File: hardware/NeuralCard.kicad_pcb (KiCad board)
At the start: 2 copper layers, 85.6 x 54 mm, 66 parts, among them J1 ProgPads, J2 TYPE-C-31-M-12, Q1 AO3401A, SW1 SW-SMD_4P-L5.1-W5.1-P3.70-LS6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, SW2 SW-SMD_4P-L5.1-W5.1-P3.70-LS6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, SW3 SW_SPDT_Shouhan_MSK12C02, U1 WIRELM-SMD_ESP32-S3-WROOM-1, U2 LGA-14_L3.0-W2.5-P0.50-TL, U3 ME6211C33M5G-N, U4 SO-8_L4.9-W3.9-P1.27-LS5.9-BL, U5 USBLC6-2SC6

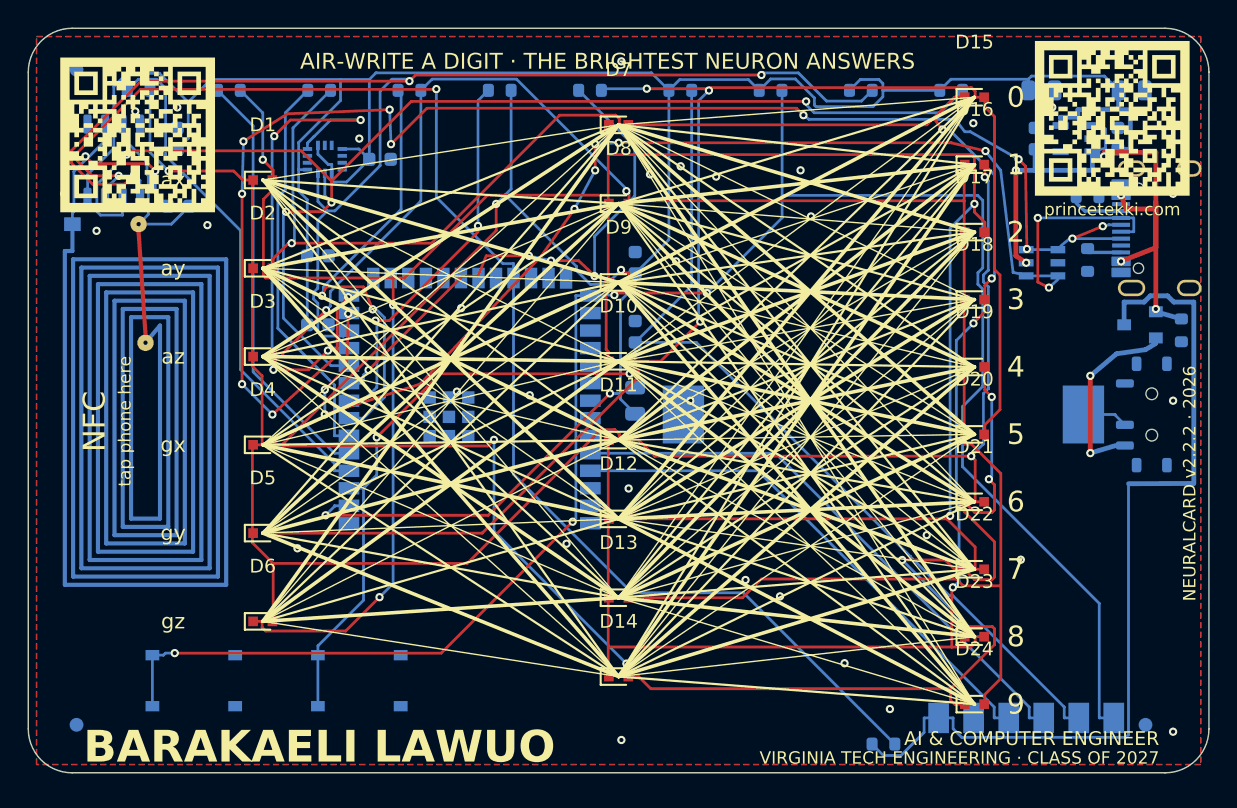
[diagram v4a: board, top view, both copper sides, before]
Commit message: bridge gnd islands
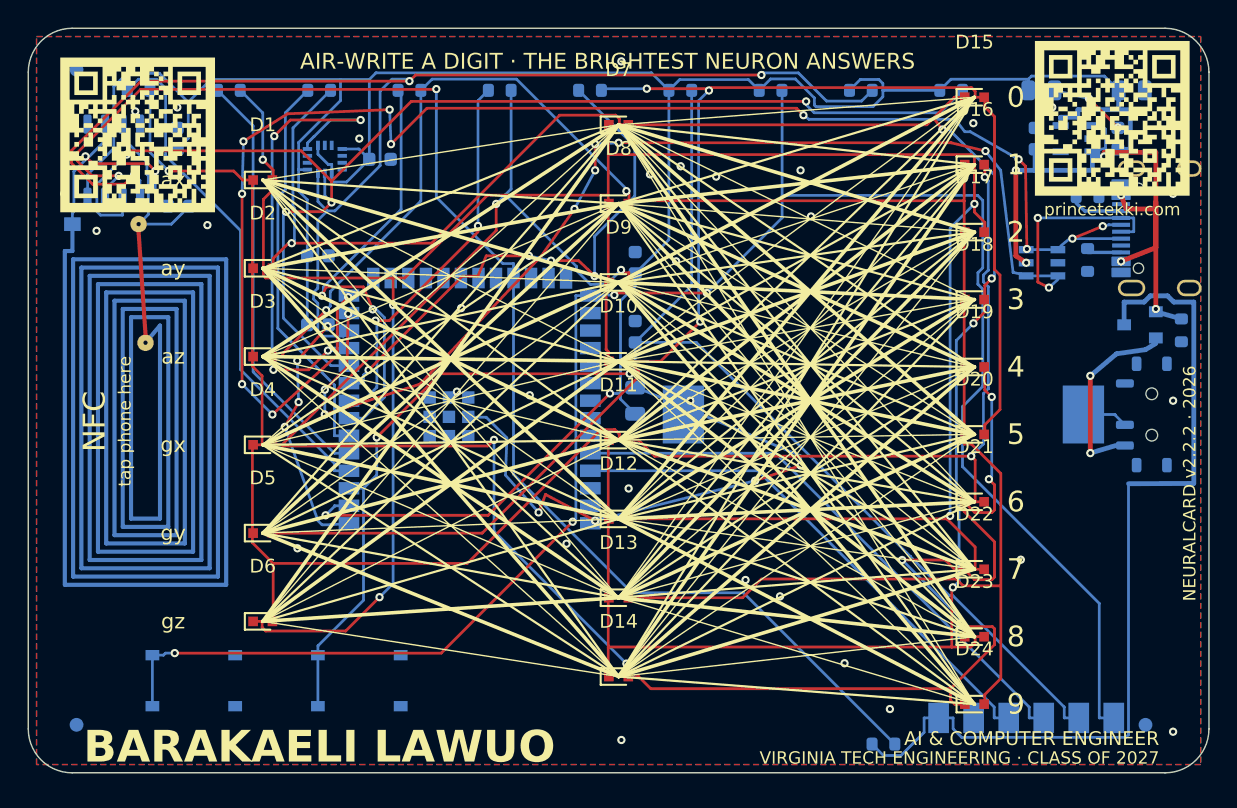
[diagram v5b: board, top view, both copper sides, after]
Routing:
- net GND: track 0.00 -> 67.9 mm, vias 32 -> 41
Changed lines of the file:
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@@
 			)
 		)
-		(clearance 0.09)
+		(clearance 0.1)
 		(attr smd)
 		(duplicate_pad_numbers_are_jumpers no)
@@
 		(net "USB_DP")
 	)
+	(segment
+		(start 56 31.7)
+		(end 52.7 32.8)
+		(width 0.2)
+		(layer "F.Cu")
+		(net "GND")
+	)
+	(segment
+		(start 21.7 21.6)
+		(end 19.5 24.1)
+		(width 0.2)
+		(layer "F.Cu")
+		(net "GND")
+	)
+	(segment
+		(start 41.1 35.7)
+		(end 37.5 33.8)
+		(width 0.2)
+		(layer "F.Cu")
+		(net "GND")
+	)
+	(segment
+		(start 19.6 27.1)
+		(end 18.6 28.9)
+		(width 0.2)
+		(layer "F.Cu")
+		(net "GND")
+	)
+	(segment
+		(start 37.5 33.8)
+		(end 37 35.1)
+		(width 0.2)
+		(layer "F.Cu")
+		(net "GND")
+	)
+	(segment
+		(start 79 7.2)
+		(end 76.9 5.1)
+		(width 0.2)
+		(layer "F.Cu")
+		(net "GND")
+	)
+	(via
+		(at 76.9 5.1)
+		(size 0.6)
+		(drill 0.3)
+		(layers "F.Cu" "B.Cu")
+		(net "GND")
+	)
 	(via
 		(at 10.806 5.734)
@@
 	)
 	(via
+		(at 79 7.2)
+		(size 0.6)
+		(drill 0.3)
+		(layers "F.Cu" "B.Cu")
+		(net "GND")
+	)
+	(via
 		(at 43 2.4)
 		(size 0.6)
@@
 	)
 	(via
+		(at 37 35.1)
+		(size 0.6)
+		(drill 0.3)
+		(layers "F.Cu" "B.Cu")
+		(net "GND")
+	)
+	(via
 		(at 7.758 6.026)
 		(size 0.6)
@@
 	)
 	(via
-		(at 65.139356 36.750118)
+		(at 43 51.6)
+		(size 0.6)
+		(drill 0.3)
+		(layers "F.Cu" "B.Cu")
+		(net "GND")
+	)
+	(via
+		(at 19.6 27.1)
 		(size 0.6)
 		(drill 0.3)
@@
 	)
 	(via
-		(at 43 51.6)
+		(at 52.7 32.8)
+		(size 0.6)
+		(drill 0.3)
+		(layers "F.Cu" "B.Cu")
+		(net "GND")
+	)
+	(via
+		(at 41.1 35.7)
 		(size 0.6)
 		(drill 0.3)
@@
 	)
 	(via
+		(at 19.5 24.1)
+		(size 0.6)
+		(drill 0.3)
+		(layers "F.Cu" "B.Cu")
+		(net "GND")
+	)
+	(via
 		(at 4.95 14.684853)
 		(size 0.6)
@@
 	)
 	(via
+		(at 56 31.7)
+		(size 0.6)
+		(drill 0.3)
+		(layers "F.Cu" "B.Cu")
+		(net "GND")
+	)
+	(via
 		(at 45.07617 10.588544)
 		(size 0.6)
@@
 	)
 	(via
+		(at 18.6 28.9)
+		(size 0.6)
+		(drill 0.3)
+		(layers "F.Cu" "B.Cu")
+		(net "GND")
+	)
+	(via
 		(at 36.355615 26.605528)
 		(size 0.6)
@@
 	)
 	(via
+		(at 21.7 21.6)
+		(size 0.6)
+		(drill 0.3)
+		(layers "F.Cu" "B.Cu")
+		(net "GND")
+	)
+	(via
 		(at 39.025 37.369)
 		(size 0.6)
@@
 		(net "GND")
 	)
+	(segment
+		(start 34.6 32.4)
+		(end 34.7 29.7)
+		(width 0.2)
+		(layer "B.Cu")
+		(net "GND")
+	)
+	(segment
+		(start 21.8 21.5)
+		(end 21.7 21.6)
+		(width 0.2)
+		(layer "B.Cu")
+		(net "GND")
+	)
+	(segment
+		(start 37 35.1)
+		(end 34.6 32.4)
+		(width 0.2)
+		(layer "B.Cu")
+		(net "GND")
+	)
+	(segment
+		(start 33.2 28.2)
+		(end 31.9 28.2)
+		(width 0.2)
+		(layer "B.Cu")
+		(net "GND")
+	)
+	(segment
+		(start 56 31)
+		(end 56 31.7)
+		(width 0.2)
+		(layer "B.Cu")
+		(net "GND")
+	)
+	(segment
+		(start 21.3 36)
+		(end 21.9 36)
+		(width 0.2)
+		(layer "B.Cu")
+		(net "GND")
+	)
+	(segment
+		(start 52.7 32.8)
+		(end 41.1 35.7)
+		(width 0.2)
+		(layer "B.Cu")
+		(net "GND")
+	)
+	(segment
+		(start 76.9 5.1)
+		(end 74.4 4.5)
+		(width 0.2)
+		(layer "B.Cu")
+		(net "GND")
+	)
+	(segment
+		(start 34.7 29.7)
+		(end 33.2 28.2)
+		(width 0.2)
+		(layer "B.Cu")
+		(net "GND")
+	)
+	(segment
+		(start 18.6 28.9)
+		(end 21 35.7)
+		(width 0.2)
+		(layer "B.Cu")
+		(net "GND")
+	)
+	(segment
+		(start 21 35.7)
+		(end 21.3 36)
+		(width 0.2)
+		(layer "B.Cu")
+		(net "GND")
+	)
+	(segment
+		(start 21.9 36)
+		(end 23.2 35.9)
+		(width 0.2)
+		(layer "B.Cu")
+		(net "GND")
+	)
+	(segment
+		(start 19.5 24.1)
+		(end 19.6 27.1)
+		(width 0.2)
+		(layer "B.Cu")
+		(net "GND")
+	)
+	(segment
+		(start 44 26)
+		(end 56 31)
+		(width 0.2)
+		(layer "B.Cu")
+		(net "GND")
+	)

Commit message: solve all drc violations
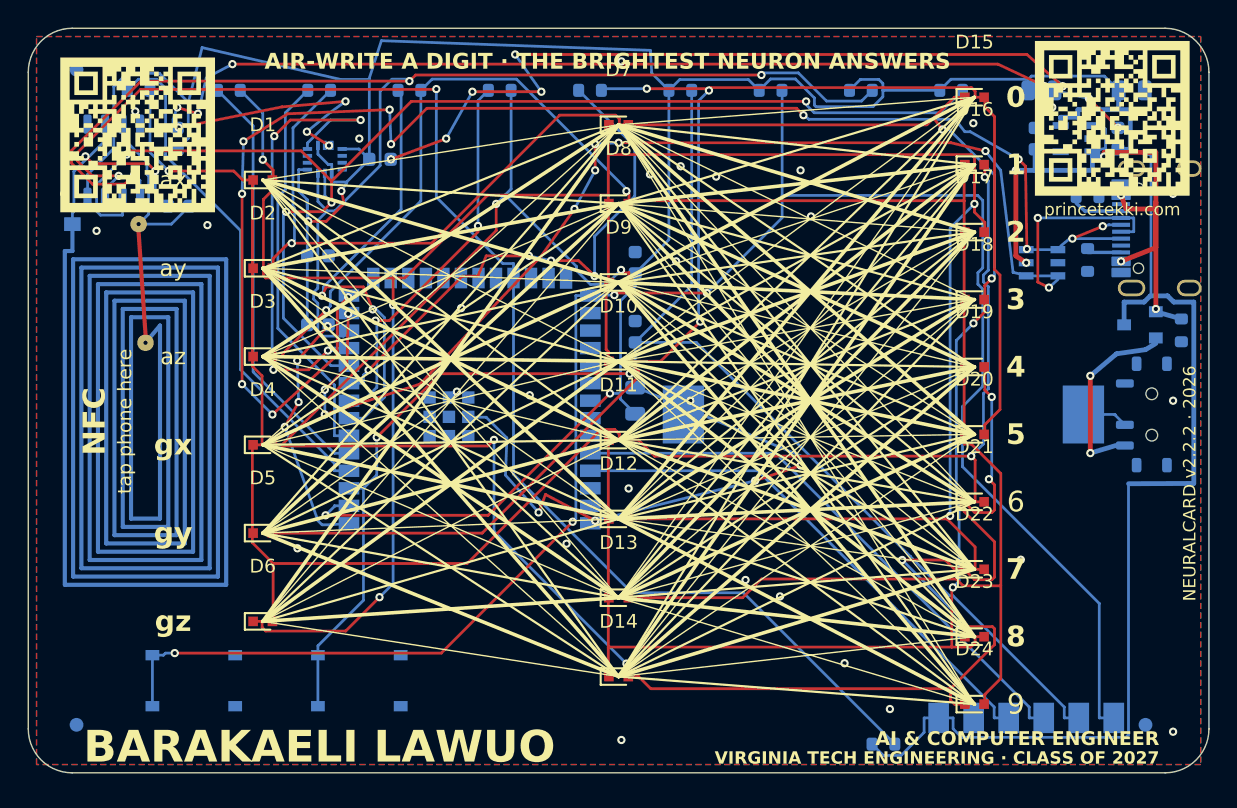
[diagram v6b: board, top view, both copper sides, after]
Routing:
- net GND: track 67.9 -> 211.9 mm, vias 41 -> 54
- net +3V3: track 258.7 -> 275.7 mm, vias 2 -> 4

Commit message: bump version to v2.3
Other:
- board text added: "NEURALCARD v2.3 · 2026"
- board text added: "NeuralCard v2.3 · princetekki.com"
- board text removed: "NEURALCARD v2.2.2 · 2026"
- board text removed: "NeuralCard v2.2.2 · princetekki.com"
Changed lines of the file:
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@@
 	)
 	(paper "A3")
+	(title_block
+		(title "NeuralCard")
+		(date "2026-08-07")
+		(rev "v2.3")
+	)
 	(layers
 		(0 "F.Cu" signal)
@@
 		)
 	)
-	(gr_text "NEURALCARD v2.2.2 · 2026"
+	(gr_text "NEURALCARD v2.3 · 2026"
 		(at 84.2 33 90)
 		(layer "F.SilkS")
@@
 		)
 	)
-	(gr_text "NeuralCard v2.2.2 · princetekki.com"
+	(gr_text "NeuralCard v2.3 · princetekki.com"
 		(at 63 41.7 0)
 		(layer "B.SilkS")
